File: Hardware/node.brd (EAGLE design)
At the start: 100 x 80 mm, 47 parts, among them J1 USB_B, M1 SERVO, M2 SERVO, Q1 16MHz, U1 MAX3485CSA

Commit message: Schematic v2
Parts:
- moved C10 108.4 mm to (48.9, 31.8), turned to 180 degrees
- moved LED6 102.1 mm to (50.8, 44.5), turned to 270 degrees
- moved LED1 97.9 mm to (50.8, 47.0), turned to 270 degrees
- moved R1 95.2 mm to (35.6, 59.7)
- moved C9 92.0 mm to (35.6, 31.8)
- moved R13 90.9 mm to (47.0, 44.5), turned to 180 degrees
- moved C6 89.0 mm to (44.5, 33.7), turned to 90 degrees
- moved C7 88.2 mm to (41.9, 41.9)
- moved C8 83.2 mm to (33.0, 41.9)
- moved R10 79.2 mm to (47.0, 47.0), turned to 180 degrees
- moved C4 75.0 mm to (35.6, 29.2), turned to 90 degrees
- moved C2 73.9 mm to (41.9, 29.2), turned to 270 degrees
- moved C5 73.1 mm to (33.0, 38.1)
- moved C3 66.3 mm to (33.0, 36.8)
- moved R9 56.0 mm to (20.3, 33.0), turned to 270 degrees
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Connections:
- removed net 3.3V: M1.2, M2.2, U1.8
- net D10: now also J4.1; no longer R13.2, U1.2, U1.3
- net D12: now also R13.2
- net D2: now also U1.2, U1.3; no longer J4.1
- net VCC: now also M1.2, M2.2, U1.8
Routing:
- net GND: track 0.00 -> 16.6 mm
- net TXO: track 0.00 -> 11.1 mm
- net D2: track 0.00 -> 9.12 mm
- net N$1: track 0.00 -> 7.76 mm
- net RXI: track 0.00 -> 6.24 mm
- net N$2: track 0.00 -> 5.64 mm
- net VCC: track 0.00 -> 4.50 mm

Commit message: Hardware pcb design
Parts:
- moved J6 53.2 mm to (3.50, 50.5), turned to 270 degrees
- moved H2 46.7 mm to (36.0, 58.0)
- moved H3 42.7 mm to (36.0, 4.00)
- moved J9 40.0 mm to (36.5, 41.0)
- moved J5 39.3 mm to (36.5, 26.0)
- moved J4 39.3 mm to (36.5, 11.0)
- moved J3 37.6 mm to (11.0, 3.50), turned to 0 degrees
- moved LED1 35.8 mm to (16.0, 38.5), turned to 180 degrees
- moved LED6 32.8 mm to (18.5, 38.5), turned to 180 degrees
- moved R10 32.5 mm to (15.0, 41.5)
- moved RESET 32.1 mm to (4.50, 12.5), turned to 270 degrees
- moved C3 31.6 mm to (13.5, 12.0), turned to 180 degrees
- moved M2 31.4 mm to (27.5, 33.0), turned to 90 degrees
- moved C8 29.1 mm to (9.00, 25.5), turned to 180 degrees
- moved C13 28.6 mm to (13.5, 9.50), turned to 180 degrees
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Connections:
- removed net D14: ATMEGA.8
- net A3: now also R13.2
- net D10: now also J5.3; no longer J4.1
- net D12: now also J4.2; no longer R13.2
- net D3: no longer J4.2
- net D4: now also J4.1; no longer J4.3
- net D5: now also M1.1; no longer J5.1
- net D6: now also J4.3; no longer J5.2
- net D7: now also M2.1; no longer J5.3
- net D8: now also J5.1; no longer M1.1
- net D9: now also J5.2; no longer M2.1
- net GND: now also J3.2; no longer J3.1
- net VCC: now also J3.1; no longer J3.2
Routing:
- net GND: track 16.6 -> 193.2 mm, vias 0 -> 5
- net VCC: track 4.50 -> 145.8 mm, vias 0 -> 6
- net +12V: track 0.00 -> 47.1 mm
- net RESET: track 0.00 -> 29.6 mm, vias 0 -> 1
- net A2: track 0.00 -> 27.3 mm
- net D4: track 0.00 -> 25.1 mm
- net A1: track 0.00 -> 22.7 mm
- net D12: track 0.00 -> 21.2 mm
- net A0: track 0.00 -> 19.9 mm
- net D11: track 0.00 -> 19.5 mm, vias 0 -> 2
- net D6: track 0.00 -> 17.0 mm
- net D10: track 0.00 -> 16.0 mm
- net D13: track 0.00 -> 15.3 mm, vias 0 -> 2
- net D8: track 0.00 -> 15.1 mm
- net D9: track 0.00 -> 14.1 mm
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- added copper zone on layer 1, net GND
- added copper zone on layer 16, net GND
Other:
- board size 100 x 80 mm -> 40 x 62 mm

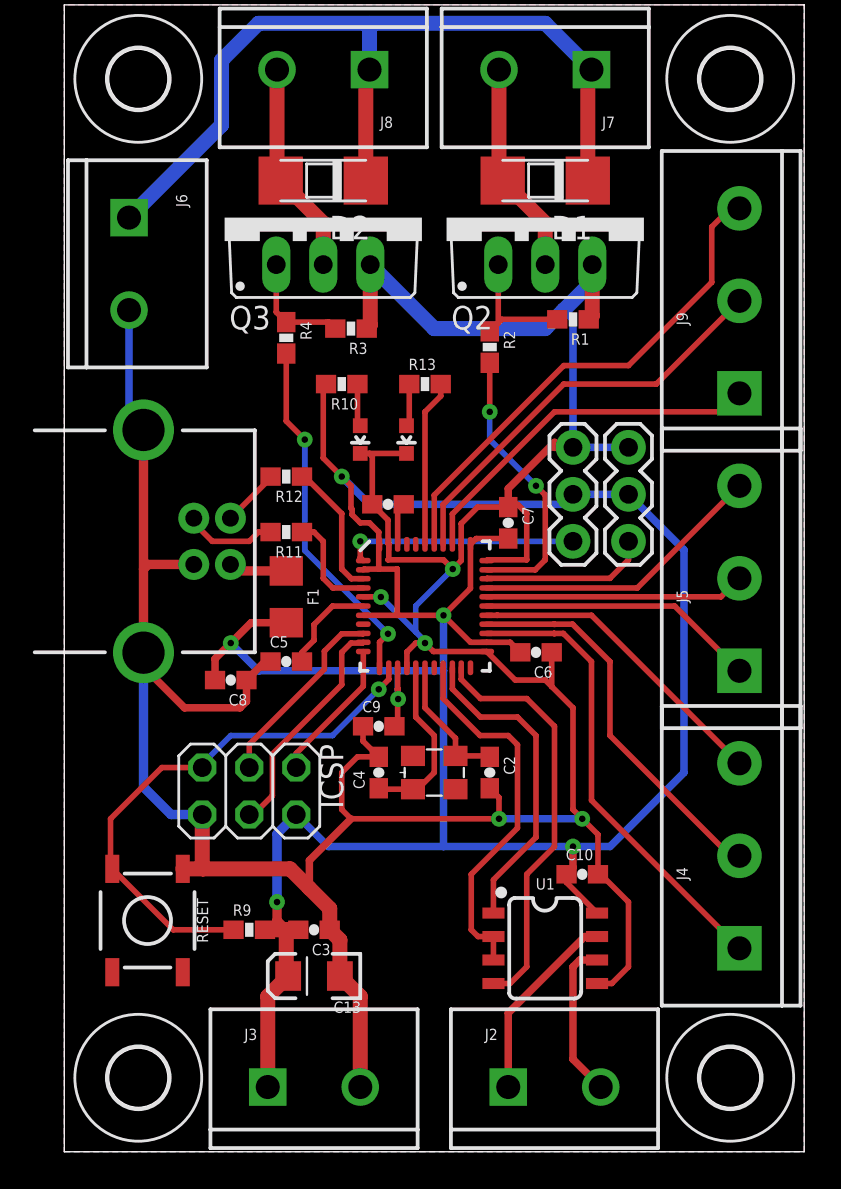
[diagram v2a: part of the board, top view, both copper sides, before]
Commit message: Finalize hardware design and add production files
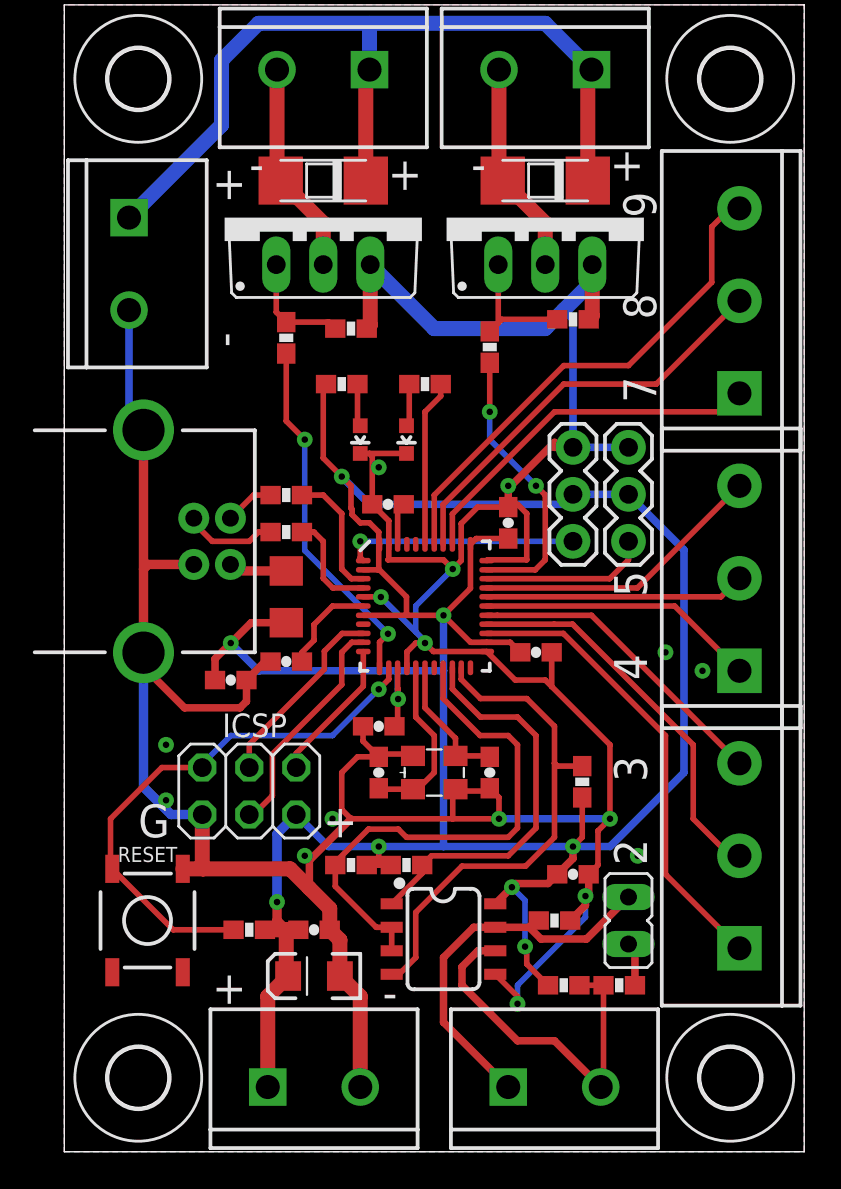
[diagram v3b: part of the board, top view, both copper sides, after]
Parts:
- added JP1: (no value), jumper:JP1
- added R14, R8: 10K, SparkFun:0603-RES
- added R15: 120, SparkFun:0603-RES
- added R5, R6, R7: 20K, SparkFun:0603-RES
- LED6: value Red -> Green
- moved U1 5.52 mm to (20.5, 11.5)
- moved R12 1.00 mm to (12.0, 35.5)
- moved C10 0.50 mm to (27.5, 15.0)
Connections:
- removed net N$5: J2.2, U1.6
- new net MODA: J2.2, R15.2, R8.2, U1.6
- new net MODB: J2.1, JP1.2, R14.1, U1.7
- net D2: now also R6.2
- net GND: now also R14.2
- net N$3: now also JP1.1, R15.1; no longer J2.1, U1.7
- net RXI: now also R5.2
- net TXO: now also R7.2
- net VCC: now also R5.1, R6.1, R7.1, R8.1
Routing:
- net MODB: track 0.00 -> 21.0 mm
- net MODA: track 0.00 -> 19.8 mm
- net VCC: track 145.8 -> 158.1 mm, vias 6 -> 9
- net GND: track 193.2 -> 205.2 mm, vias 5 -> 16
- net N$5: track 8.57 -> 0.00 mm
- net D2: track 20.4 -> 28.7 mm
- net N$3: track 10.5 -> 2.37 mm
- net TXO: track 22.5 -> 27.6 mm
- net RXI: track 17.3 -> 21.5 mm
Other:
- board text added: "+"
- board text added: "-"
- board text added: "2"
- board text added: "3"
- board text added: "4"
- board text added: "5"
- board text added: "7"
- board text added: "8"
- board text added: "9"
- board text added: "G"

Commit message: Update hardware design
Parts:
- moved C5 3.91 mm to (9.00, 24.0)
- moved C6 3.91 mm to (28.0, 24.0), turned to 90 degrees
- moved C8 2.92 mm to (6.50, 24.0), turned to 90 degrees
- moved D1 0.50 mm to (26.0, 52.0)
- moved D2 0.50 mm to (14.0, 52.0)
- moved J7 0.50 mm to (28.5, 58.0)
- moved J8 0.50 mm to (16.5, 58.0)
- moved Q2 0.50 mm to (26.0, 50.0)
- moved Q3 0.50 mm to (14.0, 50.0)
- moved R1 0.50 mm to (27.5, 44.5)
- moved R11 0.50 mm to (12.5, 33.5)
- moved R12 0.50 mm to (12.5, 35.5)
- moved R2 0.50 mm to (23.0, 43.0)
- moved R3 0.50 mm to (15.5, 44.0)
- moved R4 0.50 mm to (12.0, 43.5)
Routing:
- net N$4: track 5.35 -> 10.2 mm
- net D11: track 19.5 -> 21.2 mm
- net D-: track 6.94 -> 6.15 mm
- net D2: track 28.7 -> 29.4 mm
- net GND: track 205.2 -> 205.9 mm, vias 16 -> 19
- net VCC: track 158.1 -> 157.4 mm
- net N$8: track 5.02 -> 5.52 mm
- net N$6: track 2.69 -> 3.19 mm
- net D13: track 15.3 -> 14.8 mm
- net D+: track 5.74 -> 5.24 mm
